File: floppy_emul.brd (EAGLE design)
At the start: 99.4 x 35.5 mm, 35 parts, among them J1 POWER_JACKPTH, Q1 16MHz, SW1 ENCODER, U1 ATMEGA328P, U2 HEF4050B, U3 PCF8574T, U4 LM1117 3.3V

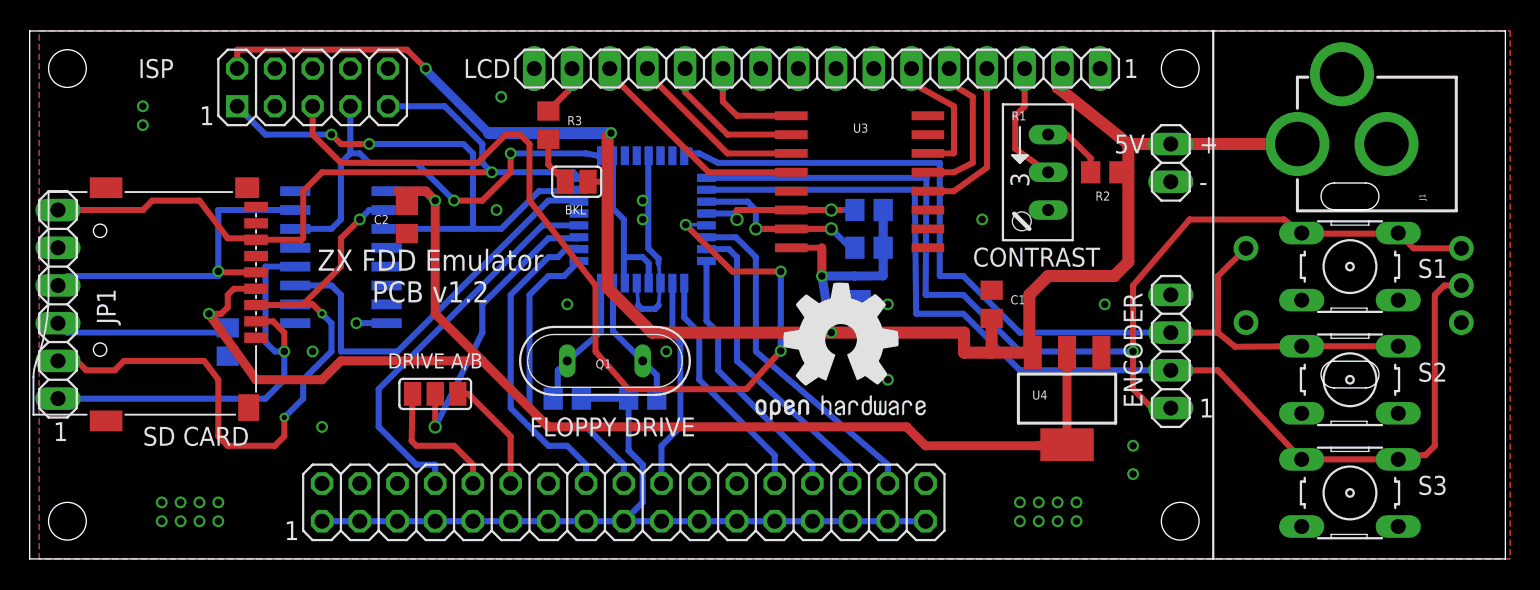
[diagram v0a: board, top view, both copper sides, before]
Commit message: new pcb revision: fixed encoder connections, small improvements
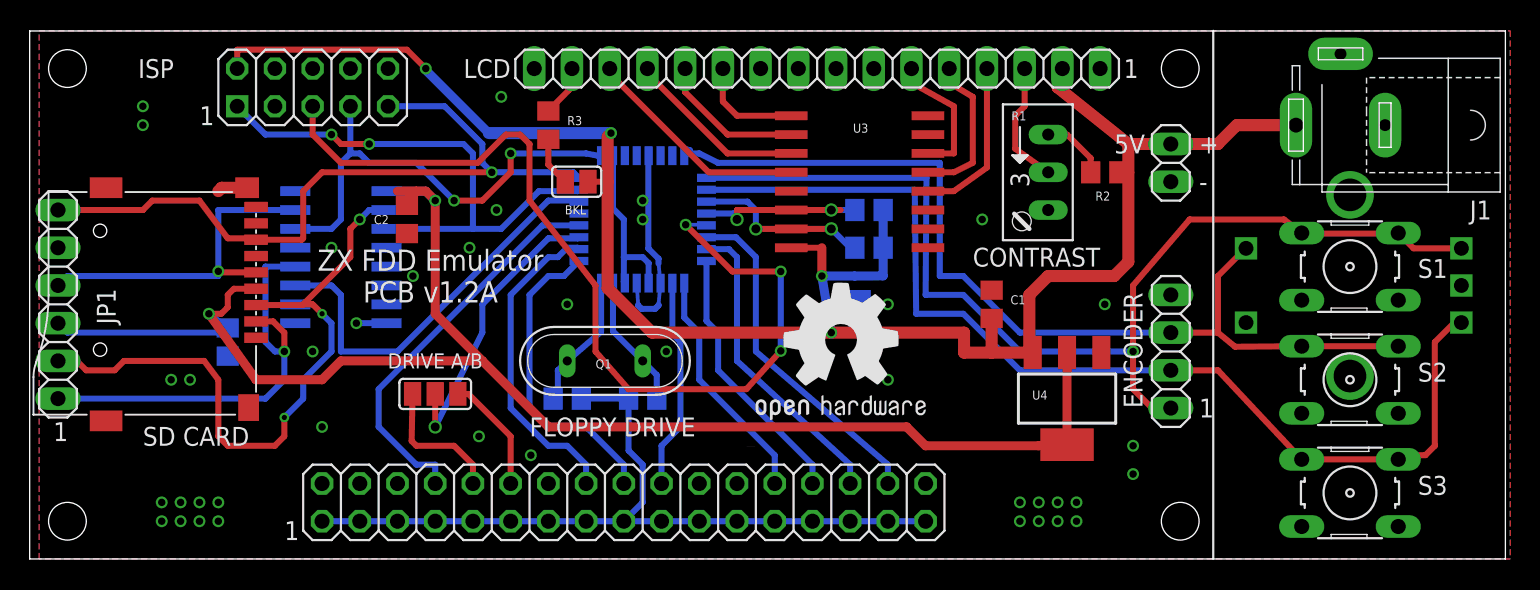
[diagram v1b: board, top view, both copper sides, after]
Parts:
- J1: value POWER_JACKPTH -> DC 5V; device SparkFun-Connectors:POWER_JACK_PTH -> con-jack:SPC4077
- S1: value (none) -> A
- S2: value (none) -> SEL
- S3: value (none) -> B
- SW1: value ENCODER -> EC12E_SW; device piher:CI-11 -> switch-alps-mod:ALPS_EC12E_SW
- moved J1 10.9 mm to (88.3, 29.2), turned to 180 degrees
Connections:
- net GND: now also J1.1, J1.2; no longer J1.GND, J1.GNDBREAK
- net VCC: now also J1.3; no longer J1.PWR
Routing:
- net ENC_B: track 74.1 -> 71.2 mm
- net GND: track 68.7 -> 70.7 mm, vias 33 -> 40
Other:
- board text added: "ZX FDD Emulator PCB v1.2A"
- board text removed: "ZX FDD Emulator PCB v1.2"
